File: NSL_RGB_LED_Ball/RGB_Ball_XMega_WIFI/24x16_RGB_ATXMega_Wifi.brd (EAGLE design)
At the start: 46.4 x 123.7 mm, 105 parts, among them IC2 TLC5947XLP, IC3 TLC5947XLP, IC4 TLC5947XLP, IC5 MCP73123, IC6 CC3000, IC7 MMA7455L, IC8 OPA344, X1 NX3225GA XC1972CT-ND

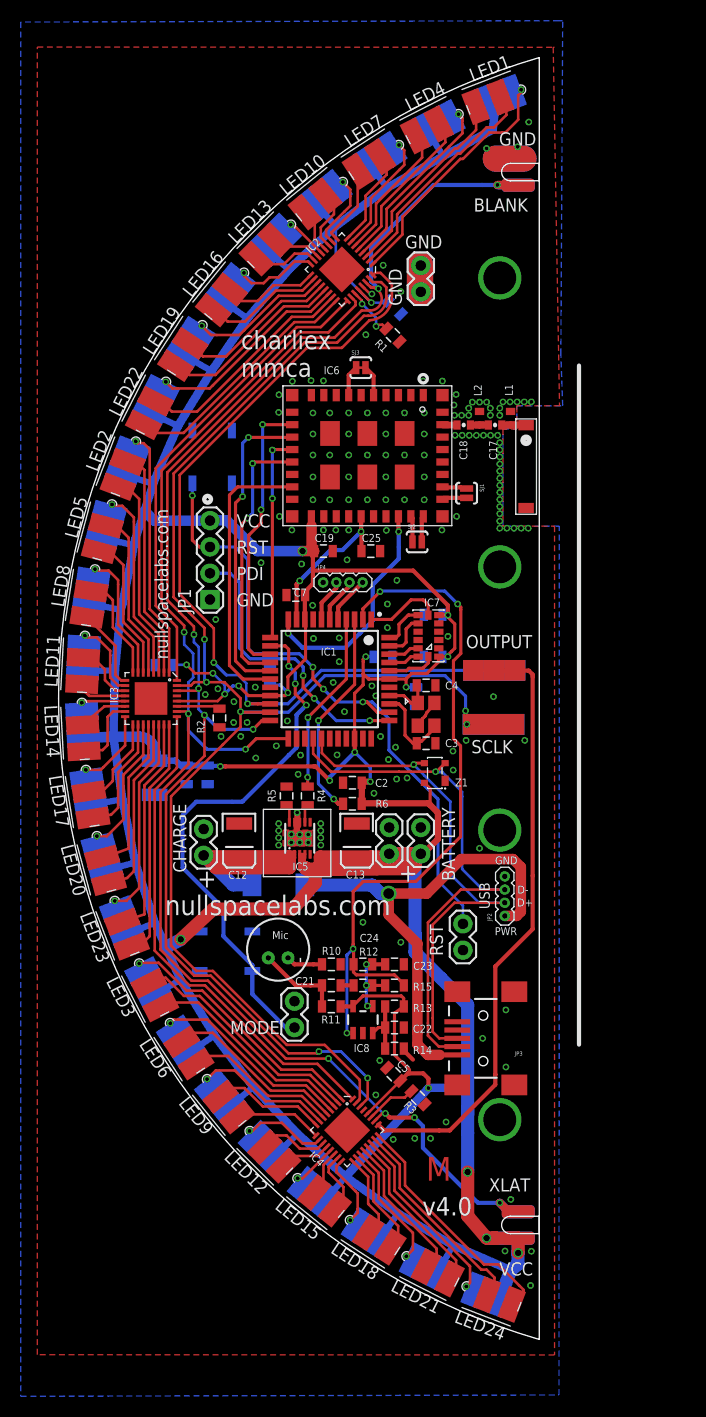
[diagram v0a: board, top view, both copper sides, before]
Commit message: 
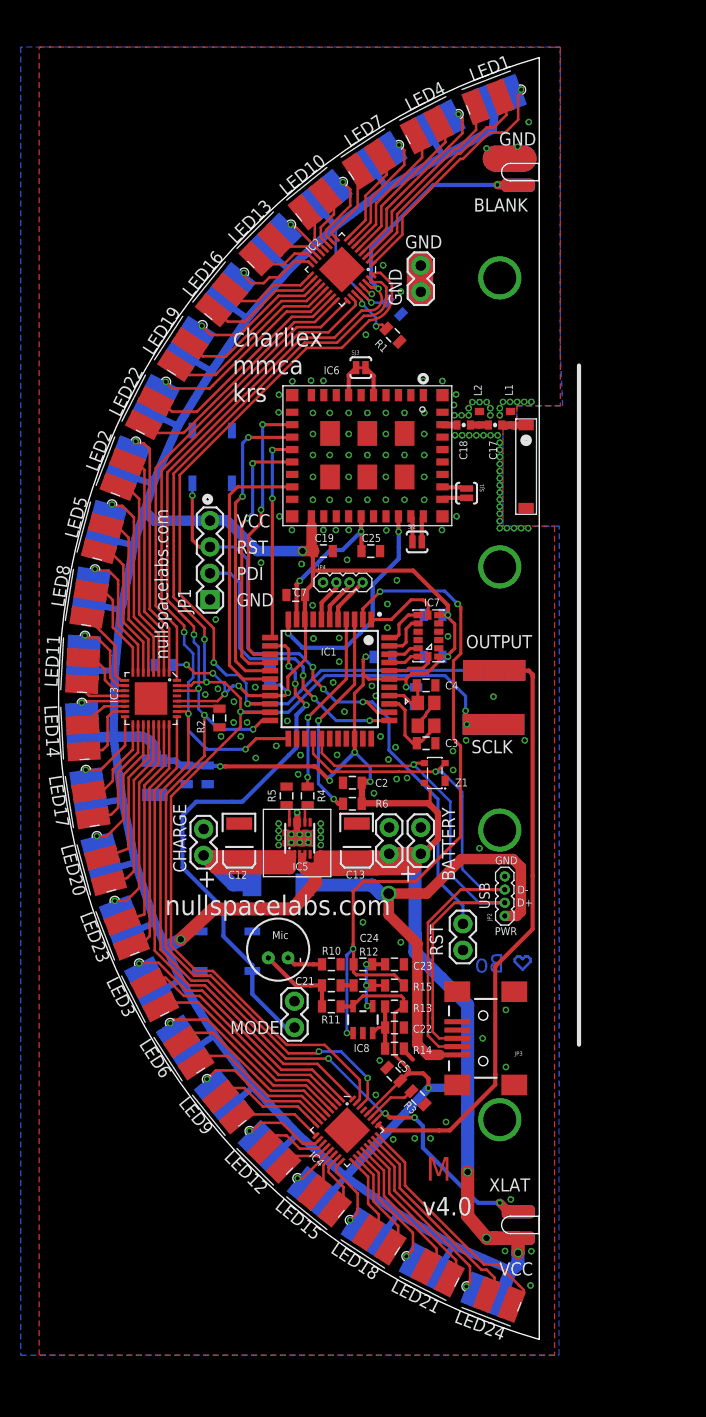
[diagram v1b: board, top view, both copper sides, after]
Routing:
- net N$18: track 0.00 -> 4.61 mm
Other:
- board text added: "Bo"
- board text added: "charliex mmca krs"
- board text removed: "charliex mmca"
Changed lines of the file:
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@@
 <layer number="21" name="tPlace" color="7" fill="1" visible="yes" active="yes"/>
 <layer number="22" name="bPlace" color="7" fill="1" visible="yes" active="yes"/>
-<layer number="23" name="tOrigins" color="15" fill="1" visible="yes" active="yes"/>
-<layer number="24" name="bOrigins" color="15" fill="1" visible="yes" active="yes"/>
-<layer number="25" name="tNames" color="7" fill="1" visible="yes" active="yes"/>
-<layer number="26" name="bNames" color="7" fill="1" visible="yes" active="yes"/>
+<layer number="23" name="tOrigins" color="15" fill="1" visible="no" active="yes"/>
+<layer number="24" name="bOrigins" color="15" fill="1" visible="no" active="yes"/>
+<layer number="25" name="tNames" color="7" fill="1" visible="no" active="yes"/>
+<layer number="26" name="bNames" color="7" fill="1" visible="no" active="yes"/>
 <layer number="27" name="tValues" color="7" fill="1" visible="no" active="yes"/>
 <layer number="28" name="bValues" color="7" fill="1" visible="no" active="yes"/>
@@
 <layer number="44" name="Drills" color="7" fill="1" visible="no" active="yes"/>
 <layer number="45" name="Holes" color="7" fill="1" visible="no" active="yes"/>
-<layer number="46" name="Milling" color="3" fill="1" visible="yes" active="yes"/>
+<layer number="46" name="Milling" color="3" fill="1" visible="no" active="yes"/>
 <layer number="47" name="Measures" color="7" fill="1" visible="no" active="yes"/>
-<layer number="48" name="Document" color="7" fill="1" visible="yes" active="yes"/>
+<layer number="48" name="Document" color="7" fill="1" visible="no" active="yes"/>
 <layer number="49" name="Reference" color="7" fill="1" visible="no" active="yes"/>
 <layer number="50" name="dxf" color="7" fill="1" visible="no" active="yes"/>
-<layer number="51" name="tDocu" color="7" fill="1" visible="yes" active="yes"/>
-<layer number="52" name="bDocu" color="7" fill="1" visible="yes" active="yes"/>
+<layer number="51" name="tDocu" color="7" fill="1" visible="no" active="yes"/>
+<layer number="52" name="bDocu" color="7" fill="1" visible="no" active="yes"/>
 <layer number="53" name="tGND_GNDA" color="7" fill="1" visible="no" active="yes"/>
 <layer number="54" name="bGND_GNDA" color="7" fill="1" visible="no" active="yes"/>
@@
 <text x="-18.542" y="46.99" size="1.27" layer="22" font="vector" rot="MR0">BLANK</text>
 <text x="-18.4404" y="53.3654" size="1.27" layer="22" font="vector" rot="MR0">GND</text>
-<text x="-46.5582" y="31.0388" size="1.778" layer="21" font="vector">charliex
-mmca</text>
+<text x="-47.371" y="28.6258" size="1.778" layer="21" font="vector">charliex
+mmca
+krs</text>
 <wire x1="-13.9446" y1="32.131" x2="-13.9446" y2="-33.401" width="0.4064" layer="21"/>
 <text x="-27.1272" y="-20.9042" size="1.905" layer="22" font="vector" ratio="12" rot="MR0">nullspacelabs.com</text>
@@
 <wire x1="-17.78" y1="-61.849" x2="-17.78" y2="61.849" width="0" layer="20"/>
 <circle x="-28.9814" y="30.861" radius="0.1524" width="0.8128" layer="21"/>
+<text x="-22.5806" y="-25.5524" size="1.778" layer="16" font="vector" ratio="12" rot="MR180" align="center">Bo</text>
 </plain>
 <attributes>
@@
 <wire x1="-52.8818" y1="-5.9954" x2="-54.8894" y2="-5.9954" width="0.6096" layer="16"/>
 <wire x1="-49.784" y1="-6.466" x2="-51.816" y2="-6.466" width="0.6096" layer="16"/>
-<wire x1="-54.8132" y1="-5.9192" x2="-54.8894" y2="-5.9954" width="0" layer="19" extent="16-16"/>
+<wire x1="-54.8132" y1="-5.9192" x2="-54.8894" y2="-5.9192" width="0.254" layer="16"/>
+<wire x1="-54.8894" y1="-5.9192" x2="-54.8894" y2="-5.9954" width="0.254" layer="16"/>
 </signal>
 <signal name="COL2">
@@
 <wire x1="-51.2572" y1="15.2908" x2="-50.5968" y2="14.6304" width="0.3048" layer="1"/>
 <wire x1="-50.5968" y1="14.6304" x2="-49.5554" y2="14.6304" width="0.3048" layer="1"/>
-<wire x1="-27.559" y1="-17.5768" x2="-25.146" y2="-19.9898" width="0.254" layer="16"/>
-<wire x1="-25.146" y1="-19.9898" x2="-25.146" y2="-21.7424" width="0.254" layer="16"/>
+<wire x1="-27.559" y1="-17.5768" x2="-25.146" y2="-19.9898" width="0.3048" layer="16"/>
+<wire x1="-25.146" y1="-19.9898" x2="-25.146" y2="-21.7424" width="0.3048" layer="16"/>
 <wire x1="-45.9232" y1="9.3218" x2="-45.9232" y2="4.9022" width="0.3048" layer="16"/>
 <wire x1="-45.9232" y1="4.9022" x2="-45.339" y2="4.318" width="0.3048" layer="16"/>
@@
 <contactref element="JP2" pad="3"/>
 <wire x1="-28.5242" y1="-21.6154" x2="-25.3492" y2="-18.4404" width="0.254" layer="1"/>
-<wire x1="-25.3492" y1="-18.4404" x2="-21.1074" y2="-18.4404" width="0.254" layer="1"/>
+<wire x1="-25.3492" y1="-18.4404" x2="-21.1074" y2="-18.4404" width="0.3048" layer="1"/>
 <wire x1="-25.2222" y1="-9.4488" x2="-25.2222" y2="-16.4592" width="0.254" layer="16"/>
 <wire x1="-25.2222" y1="-16.4592" x2="-23.241" y2="-18.4404" width="0.254" layer="16"/>
-<wire x1="-23.241" y1="-18.4404" x2="-21.1074" y2="-18.4404" width="0.254" layer="16"/>
+<wire x1="-23.241" y1="-18.4404" x2="-21.1074" y2="-18.4404" width="0.3048" layer="16"/>
 <wire x1="-28.5242" y1="-31.3182" x2="-28.5242" y2="-32.5374" width="0.254" layer="1"/>
 <wire x1="-28.5242" y1="-32.5374" x2="-27.4828" y2="-33.5788" width="0.254" layer="1"/>
@@
 <contactref element="JP2" pad="2"/>
 <wire x1="-28.067" y1="-21.8186" x2="-25.9588" y2="-19.7104" width="0.254" layer="1"/>
-<wire x1="-25.9588" y1="-19.7104" x2="-21.1074" y2="-19.7104" width="0.254" layer="1"/>
+<wire x1="-25.9588" y1="-19.7104" x2="-21.1074" y2="-19.7104" width="0.3048" layer="1"/>
 <wire x1="-28.8798" y1="-7.4168" x2="-26.3652" y2="-9.9314" width="0.254" layer="16"/>
 <wire x1="-26.3652" y1="-9.9314" x2="-26.3652" y2="-16.9418" width="0.254" layer="16"/>
 <wire x1="-26.3652" y1="-16.9418" x2="-23.5966" y2="-19.7104" width="0.254" layer="16"/>
-<wire x1="-23.5966" y1="-19.7104" x2="-21.1074" y2="-19.7104" width="0.254" layer="16"/>
+<wire x1="-23.5966" y1="-19.7104" x2="-21.1074" y2="-19.7104" width="0.3048" layer="16"/>
 <wire x1="-28.067" y1="-30.8356" x2="-28.067" y2="-32.1564" width="0.254" layer="1"/>
 <wire x1="-28.067" y1="-32.1564" x2="-27.432" y2="-32.7914" width="0.254" layer="1"/>
@@
 <polygon width="0.3048" layer="1">
 <vertex x="-16.3068" y="62.8396"/>
-<vertex x="-16.4338" y="62.8396"/>
-<vertex x="-15.8242" y="28.2448"/>
+<vertex x="-15.748" y="62.8396"/>
+<vertex x="-15.748" y="28.2448"/>
 <vertex x="-19.9898" y="28.2448"/>
 <vertex x="-19.939" y="28.1686"/>
@@
 <vertex x="-21.2852" y="16.637"/>
 <vertex x="-16.3068" y="16.637"/>
-<vertex x="-16.3068" y="-63.3476"/>
-<vertex x="-66.2178" y="-63.3222"/>
-<vertex x="-66.2178" y="62.865"/>
+<vertex x="-16.3068" y="-63.373"/>
+<vertex x="-66.04" y="-63.373"/>
+<vertex x="-66.04" y="62.865"/>
 </polygon>
 <polygon width="0.254" layer="16">
-<vertex x="-67.818" y="65.278"/>
-<vertex x="-67.818" y="-67.3354"/>
-<vertex x="-15.875" y="-67.2084"/>
+<vertex x="-67.818" y="62.865"/>
+<vertex x="-67.818" y="-63.373"/>
+<vertex x="-15.875" y="-63.373"/>
 <vertex x="-15.8496" y="16.637"/>
 <vertex x="-21.2852" y="16.637"/>
@@
 <vertex x="-19.939" y="28.2448"/>
 <vertex x="-15.5194" y="28.2448"/>
-<vertex x="-15.6972" y="33.2232"/>
-<vertex x="-15.5194" y="65.405"/>
-<vertex x="-15.875" y="65.405"/>
+<vertex x="-15.748" y="33.2232"/>
+<vertex x="-15.748" y="62.865"/>
 </polygon>
 <contactref element="BATTERY1" pad="1"/>
@@
 <wire x1="-37.3634" y1="10.668" x2="-37.3634" y2="11.2014" width="0.4064" layer="1"/>
 </signal>
+<signal name="N$4">
+</signal>
+<signal name="N$5">
+</signal>
+<signal name="N$18">
+<wire x1="-19.3802" y1="-25.146" x2="-19.6342" y2="-24.892" width="0.254" layer="16"/>
+<wire x1="-19.6342" y1="-24.892" x2="-19.8882" y2="-24.892" width="0.254" layer="16"/>
+<wire x1="-19.8882" y1="-24.892" x2="-20.1422" y2="-25.146" width="0.254" layer="16"/>
+<wire x1="-20.1422" y1="-25.146" x2="-20.1422" y2="-25.4" width="0.254" layer="16"/>
+<wire x1="-20.1422" y1="-25.4" x2="-19.3802" y2="-26.162" width="0.254" layer="16"/>
+<wire x1="-19.3802" y1="-26.162" x2="-18.6182" y2="-25.4" width="0.254" layer="16"/>
+<wire x1="-18.6182" y1="-25.4" x2="-18.6182" y2="-25.146" width="0.254" layer="16"/>
+<wire x1="-18.6182" y1="-25.146" x2="-18.8722" y2="-24.892" width="0.254" layer="16"/>
+<wire x1="-18.8722" y1="-24.892" x2="-19.1262" y2="-24.892" width="0.254" layer="16"/>
+<wire x1="-19.1262" y1="-24.892" x2="-19.3802" y2="-25.146" width="0.254" layer="16"/>
+</signal>
 </signals>

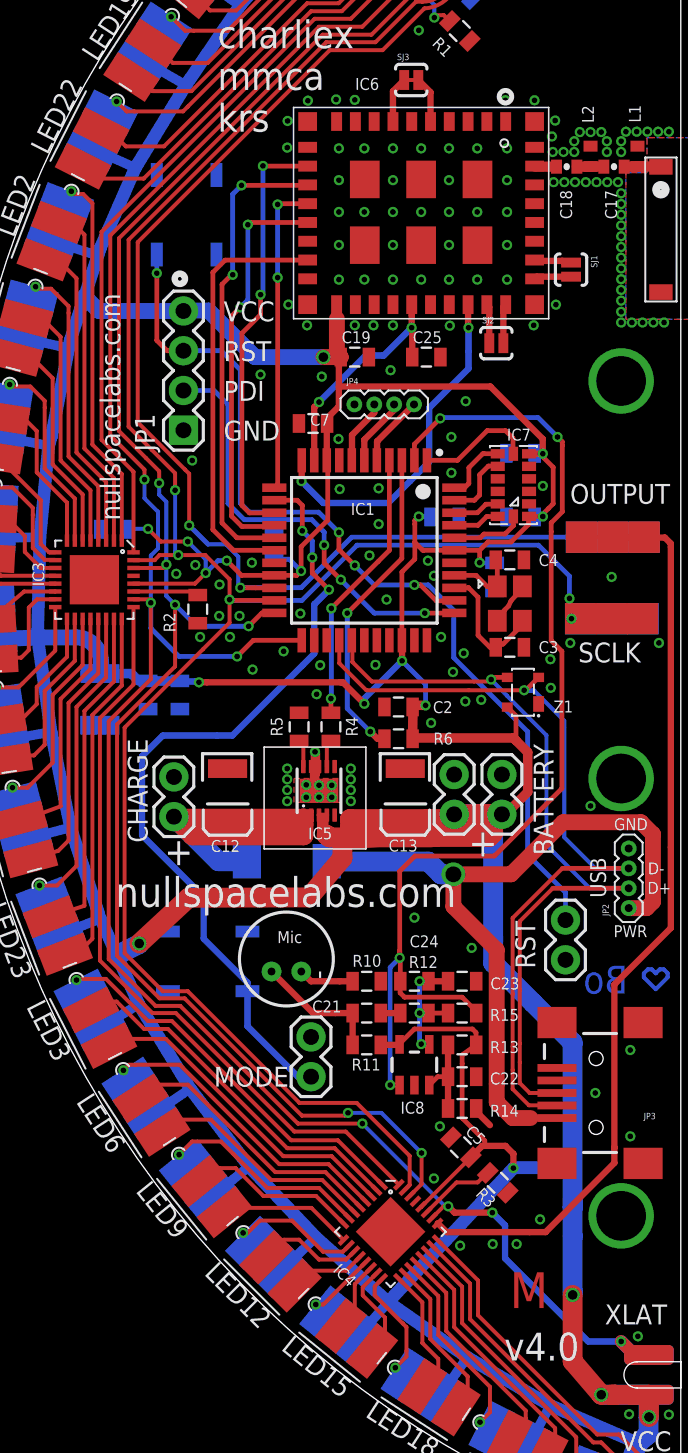
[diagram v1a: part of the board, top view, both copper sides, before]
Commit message: 
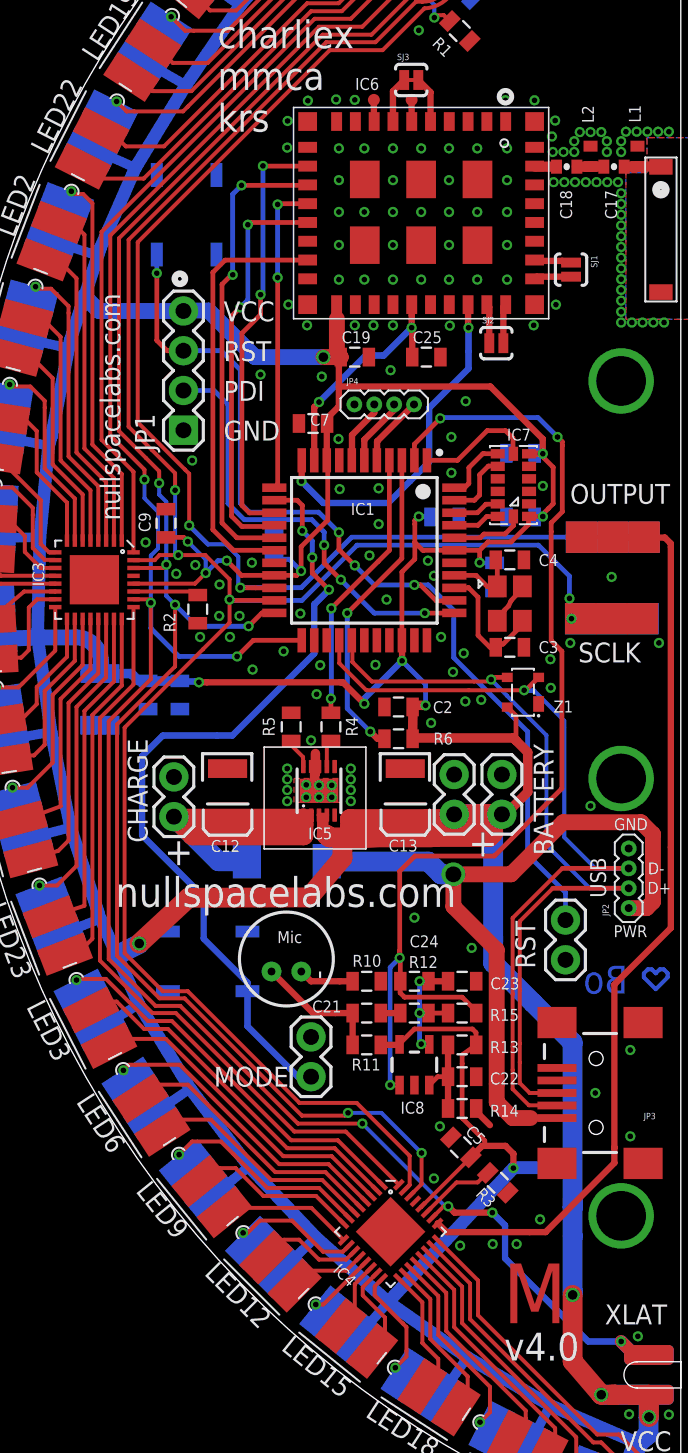
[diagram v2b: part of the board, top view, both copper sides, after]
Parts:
- added TP13, TP14: SPARKFUN_TEST-POINT3, badge.lbrbadge_2013:SPARKFUN_PAD.03X.03
- X1: value NX3225GA XC1972CT-ND -> NX3225GA-16.000M-STD-CRG-2; device M6-RF315:NX3225GA -> 24x16_RGB_ATXMega_Wifi:NX3225GA
- moved C9 3.32 mm to (-50.7, 3.61), flipped to the top, turned to 90 degrees
- moved R5 0.51 mm to (-42.7, -9.40)
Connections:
- new net N$21: IC6.P$6, TP13.P$1
- new net N$23: IC6.P$8, TP14.P$1
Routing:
- net VCC: track 555.9 -> 553.3 mm, vias 20 -> 19
- net N$23: track 0.00 -> 1.39 mm
- net N$21: track 0.00 -> 1.39 mm
- net GND: vias 166 -> 167
